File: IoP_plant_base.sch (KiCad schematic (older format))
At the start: 57 parts, among them IC1 HX711, J1 Conn_01x02, J2 Jack-DC, J4 Conn_01x02, J5 Conn_01x03, J6 Conn_01x02, J7 Conn_01x05, Q1 BC857C, Q2 IRLML6244, U1 NodeMCUv2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

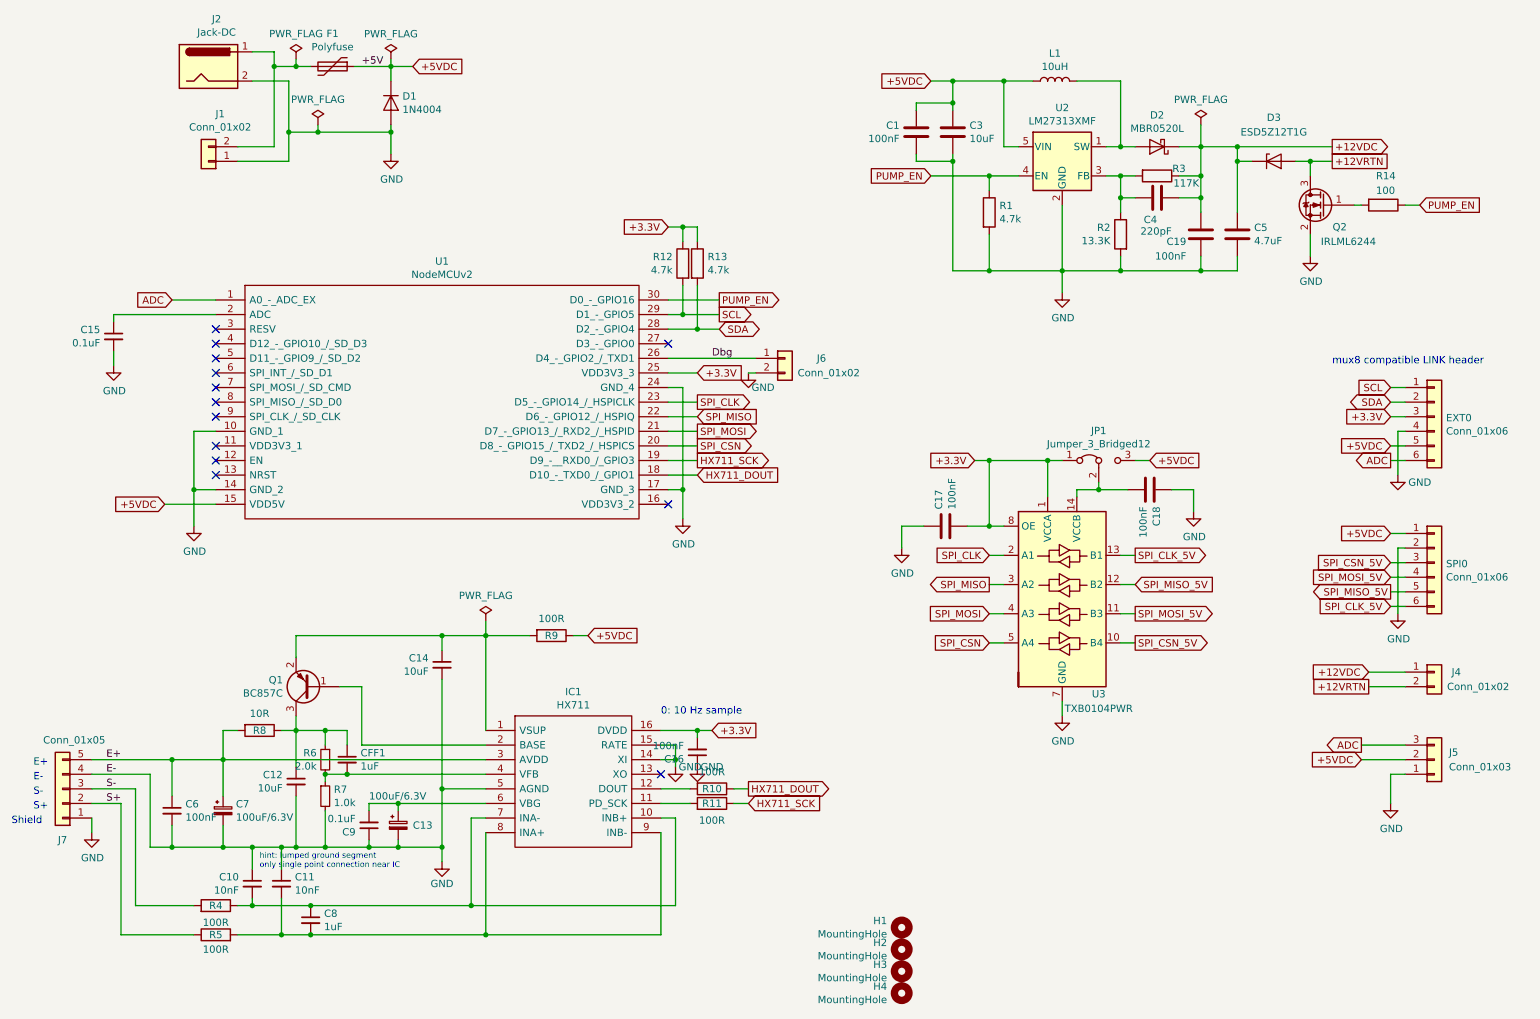
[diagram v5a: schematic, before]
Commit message: updated BOM info according to Mouser order. Note: consider migrating to ME2149F SO8 for next rev. (higher current, ~30ct vs. 1.15€)
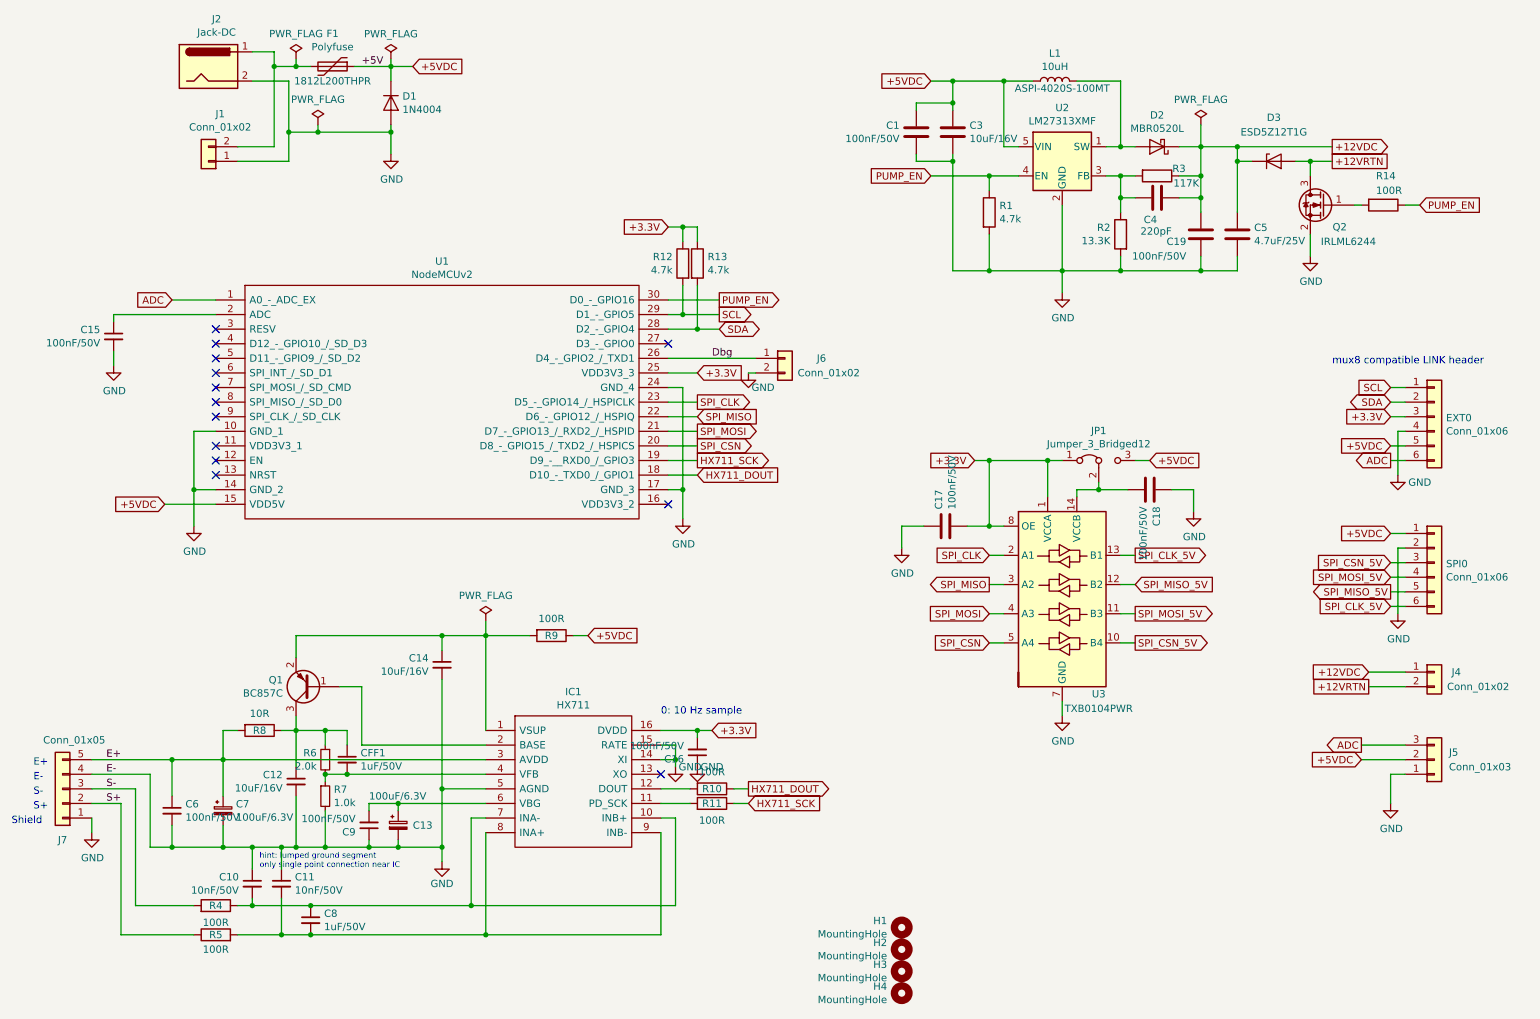
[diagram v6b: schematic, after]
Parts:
- C1, C16, C17, C18, C19, C6: value 100nF -> 100nF/50V; Mouser (none) -> 603-CC603KRX7R9BB104
- C10, C11: value 10nF -> 10nF/50V; Mouser (none) -> 710-885012206089
- C12, C14, C3: value 10uF -> 10uF/16V; Mouser (none) -> 80-C0805C475M9RAUTO
- C13, C7: MF (none) -> AVX; MPN (none) -> F930J107KBA; Mouser (none) -> 647-F930J107KBA
- C15, C9: value 0.1uF -> 100nF/50V; Mouser (none) -> 603-CC603KRX7R9BB104
- C4: Mouser (none) -> 81-GCM1885C2A221J16D
- C5: value 4.7uF -> 4.7uF/25V; Mouser (none) -> 81-GCM21BC71E475KE6L
- C8, CFF1: value 1uF -> 1uF/50V; Mouser (none) -> 963-LMK212B7225KG-T
- D2: Field6 512-MBR0520L -> (none); Mouser (none) -> 512-MBR0520L
- EXT0, SPI0: Digikey (none) -> 455-1708-ND
- J1, J4, J6: Digikey (none) -> 455-1704-ND
- J5: Digikey (none) -> 455-1705-ND
- J7: Digikey (none) -> 455-1707-ND
- L1: MPN (none) -> ASPI-4020S-100MT; MPN2 (none) -> 74438357100; Mouser (none) -> 815-ASPI-4020S-100MT; Mouser2 (none) -> 710-74438357100
- Q1: MF (none) -> On Semi; MPN (none) -> BC857CWT1G; Mouser (none) -> 863-BC857CWT1G
- R14: value 100 -> 100R
- R2: Mouser (none) -> 71-CRCW0603-13.3K-E3
- R3: Mouser (none) -> 603-RT0603DRE07117KL
- R6: Mouser (none) -> 71-CRCW0603-2.0K-E3
